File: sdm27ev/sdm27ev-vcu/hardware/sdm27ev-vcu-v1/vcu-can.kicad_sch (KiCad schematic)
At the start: 16 parts, among them IC5 MCP2518FDT-E_SL, IC6 TCAN3413DR, IC7 MCP2518FDT-E_SL, IC8 TCAN3413DR, Y1 ECS-3225MVQ-400-BS-TR, Y2 ECS-3225MVQ-400-BS-TR

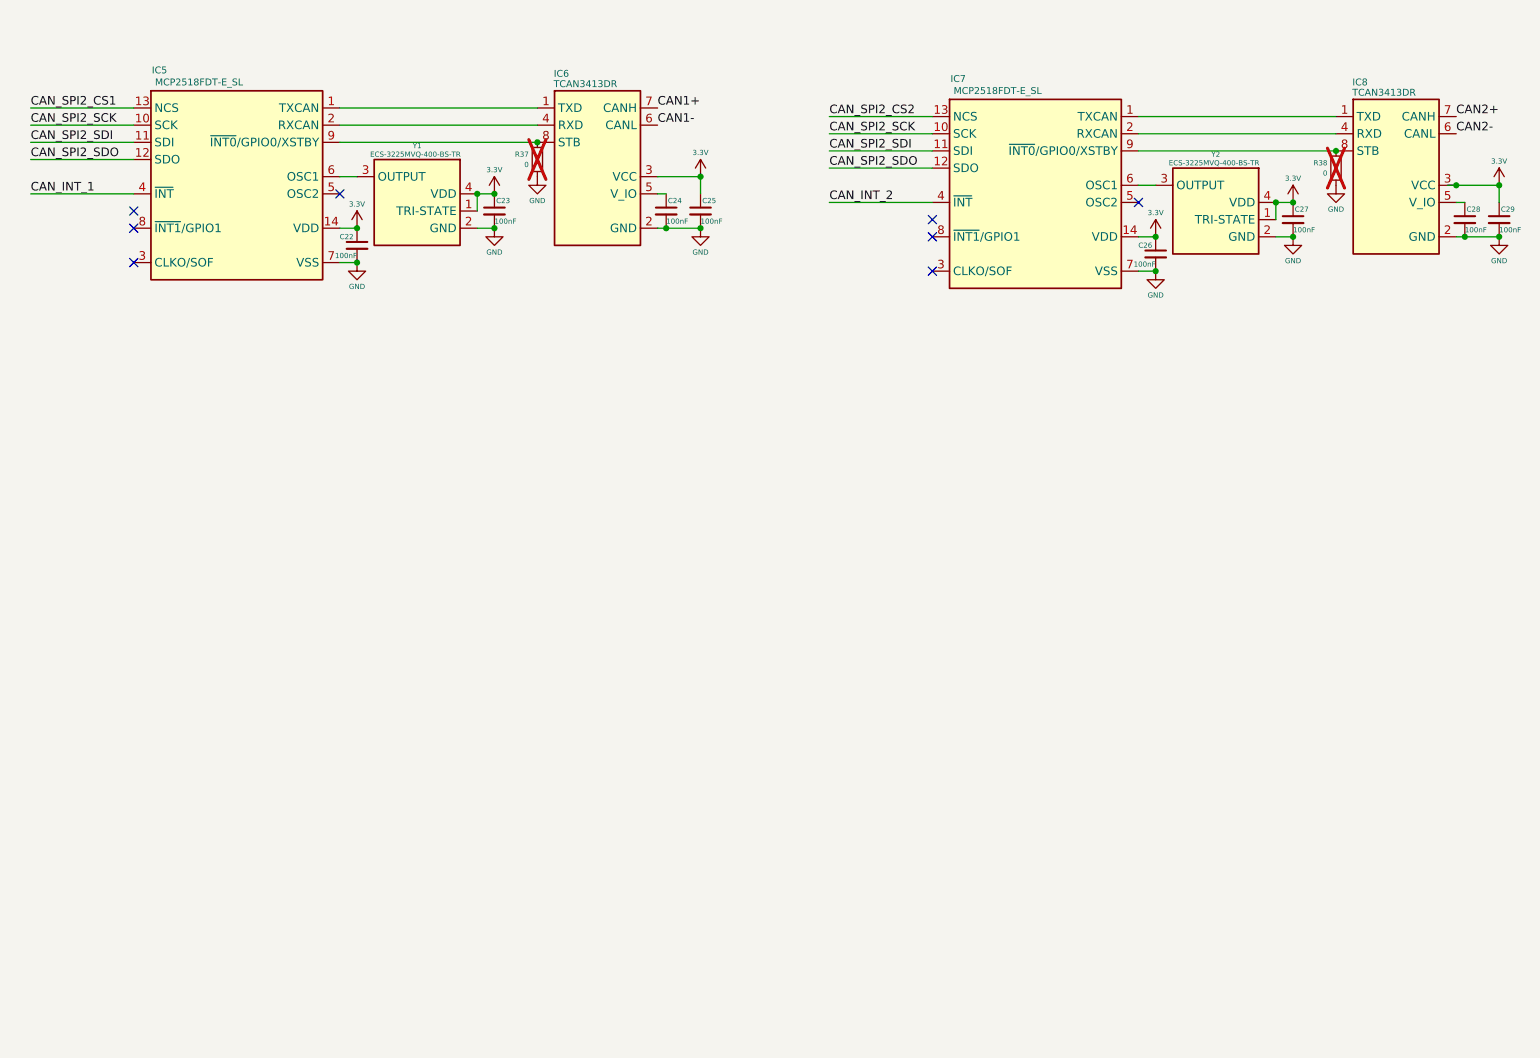
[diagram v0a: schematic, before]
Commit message: added all hierarchical sheet pins, added can termination optocouplers
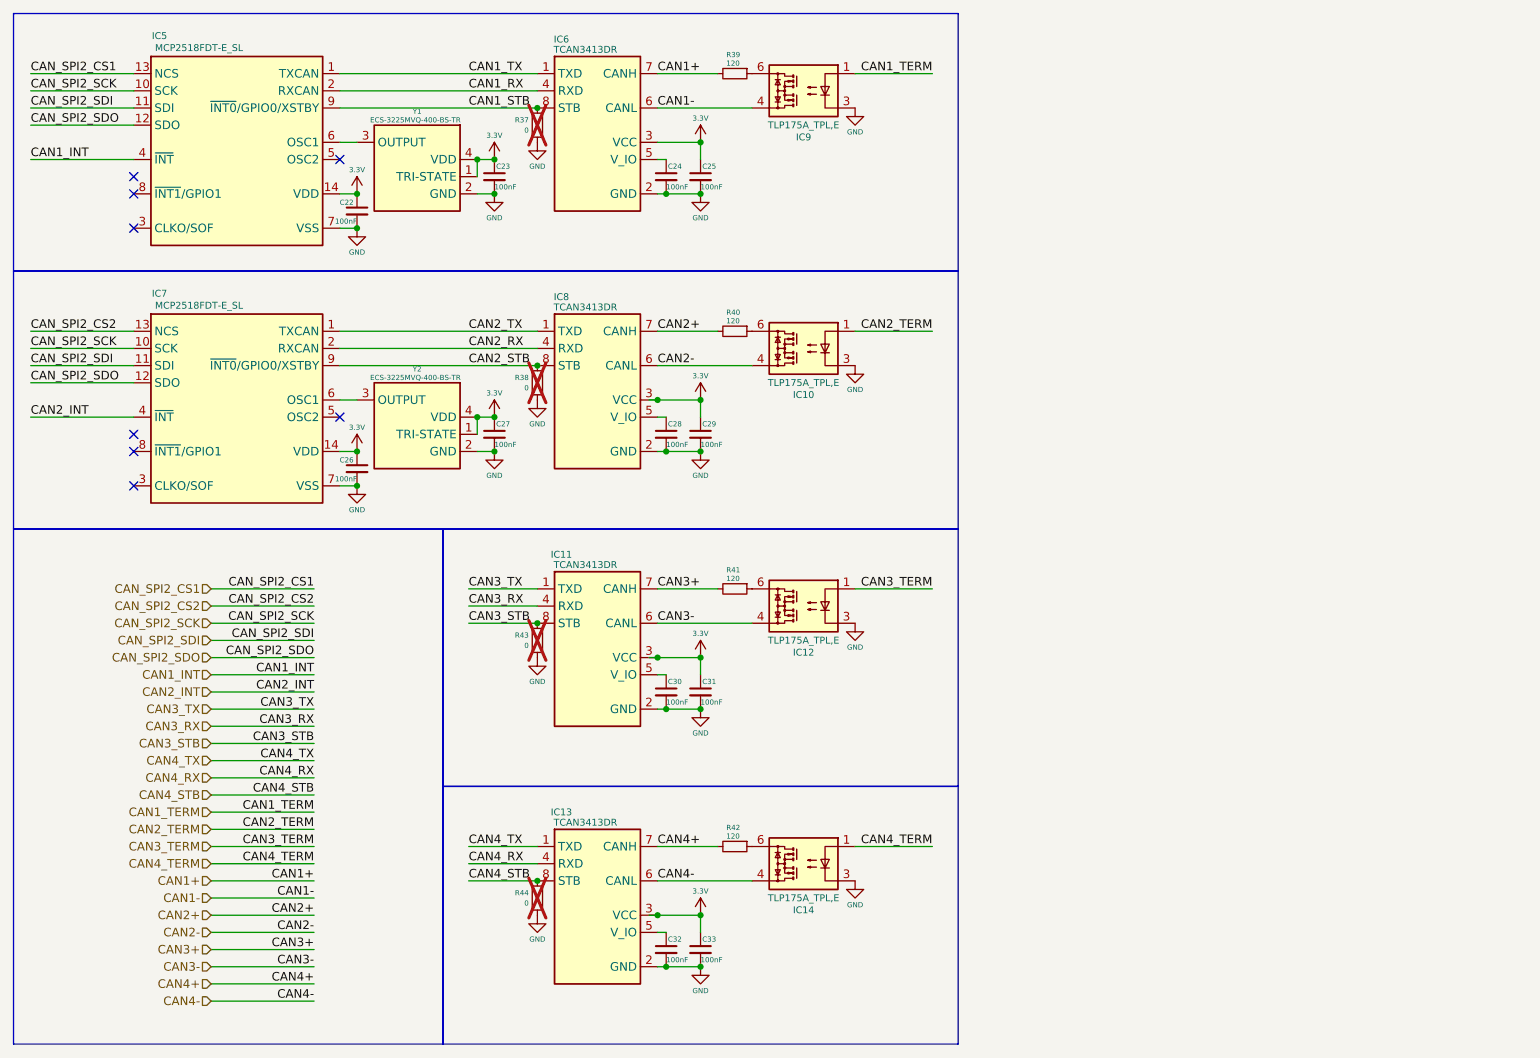
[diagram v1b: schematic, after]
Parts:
- added C30, C31, C32, C33: 100nF, Capacitor_SMD:C_0603_1608Metric, symbol Device:C_Small
- added IC10, IC12, IC14, IC9: TLP175A_TPL,E, SDM_MiscFootprint:TLP266J, symbol SDM_OPTOCOUPLERS:TLP175A_TPL,E
- added IC11, IC13: TCAN3413DR, SOIC127P600X175-8N, symbol SDM_EV:TCAN3413DR
- added R39, R40, R41, R42: 120, Resistor_SMD:R_0402_1005Metric, symbol Device:R_Small
- added R43, R44: 0, Resistor_SMD:R_0402_1005Metric, symbol Device:R_Small
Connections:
- net 3.3V: now also C31.1, C33.1, IC11.3 (VCC), IC13.3 (VCC)
- net CAN1+: now also R39.2
- net CAN1-: now also IC9.4
- net CAN2+: now also R40.2
- net CAN2-: now also IC10.4
- net GND: now also C30.2, C31.2, C32.2, C33.2, IC10.3, IC11.2 (GND), IC12.3, IC13.2 (GND), IC14.3, IC9.3, R43.1, R44.1
- net CAN2_TX: now reaches IC7.1 (TXCAN), IC8.1 (TXD)
- net CAN2_RX: now reaches IC7.2 (RXCAN), IC8.4 (RXD)
- net CAN2_STB: now reaches IC7.9 (~{INT0}/GPIO0/XSTBY), IC8.8 (STB), R38.2
- net CAN1_STB: now reaches IC5.9 (~{INT0}/GPIO0/XSTBY), IC6.8 (STB), R37.2
- net CAN1_TX: now reaches IC5.1 (TXCAN), IC6.1 (TXD)
- net CAN1_RX: now reaches IC5.2 (RXCAN), IC6.4 (RXD)
- net CAN_INT_1 renamed CAN1_INT
- net CAN_INT_2 renamed CAN2_INT
- new net: IC9.6, R39.1
- new net: IC12.6, R41.1
- new net: C32.1, IC13.5 (V_IO)
- new net: IC14.6, R42.1
- new net: C30.1, IC11.5 (V_IO)
- new net: IC10.6, R40.1
- new net CAN1_TERM: IC9.1
- new net CAN2_TERM: IC10.1
- new net CAN3+: IC11.7 (CANH), R41.2
- new net CAN3-: IC11.6 (CANL), IC12.4
- new net CAN3_RX: IC11.4 (RXD)
- new net CAN3_STB: IC11.8 (STB), R43.2
- new net CAN3_TERM: IC12.1
- new net CAN3_TX: IC11.1 (TXD)
- new net CAN4+: IC13.7 (CANH), R42.2
- new net CAN4-: IC13.6 (CANL), IC14.4
- new net CAN4_RX: IC13.4 (RXD)
- new net CAN4_STB: IC13.8 (STB), R44.2
- new net CAN4_TERM: IC14.1
- new net CAN4_TX: IC13.1 (TXD)
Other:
- moved on the sheet: C22, C23, C24, C25, C26, C27, C28, C29, IC5, IC6, IC7, IC8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

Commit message: Fixed resistor values from transceiver to optocoupler
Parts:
- R39, R40, R41, R42: value 120 -> 100
